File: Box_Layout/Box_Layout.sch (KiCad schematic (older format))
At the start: 32 parts, among them J1 Arduino_Mega_Header, X1 AMP967629, X2 DT04-12P

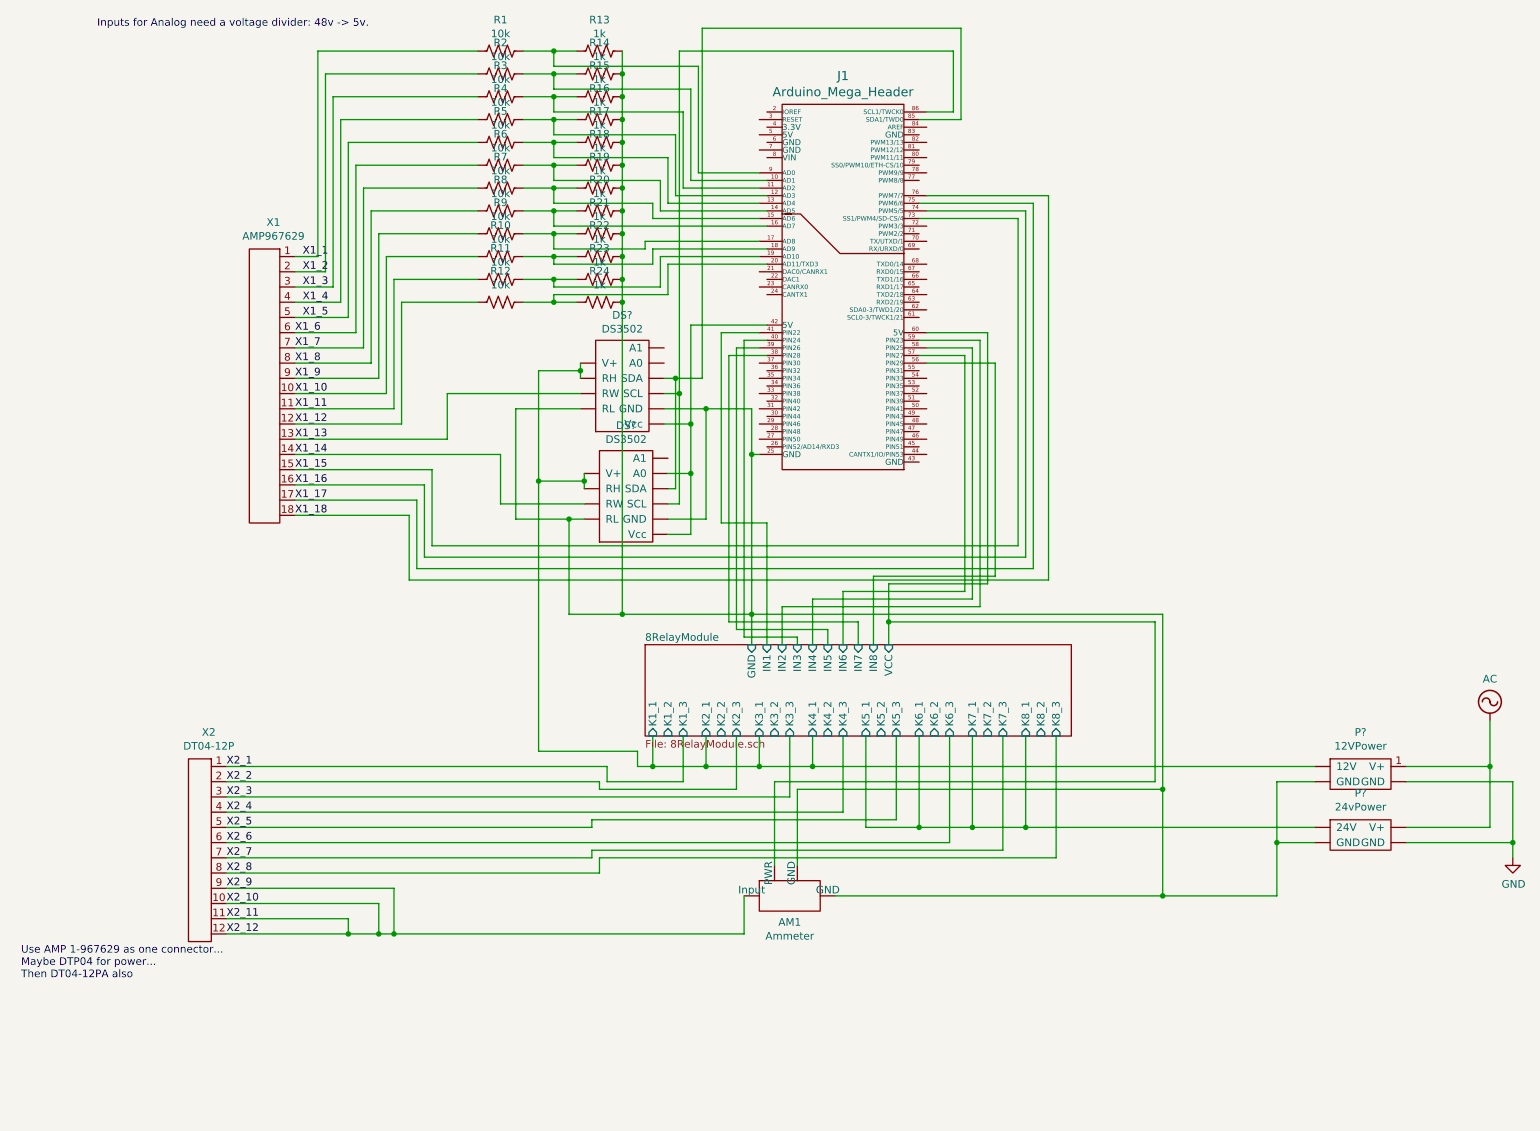
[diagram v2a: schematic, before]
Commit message: Changes to layout, and a bit to code.  Added a few tests.
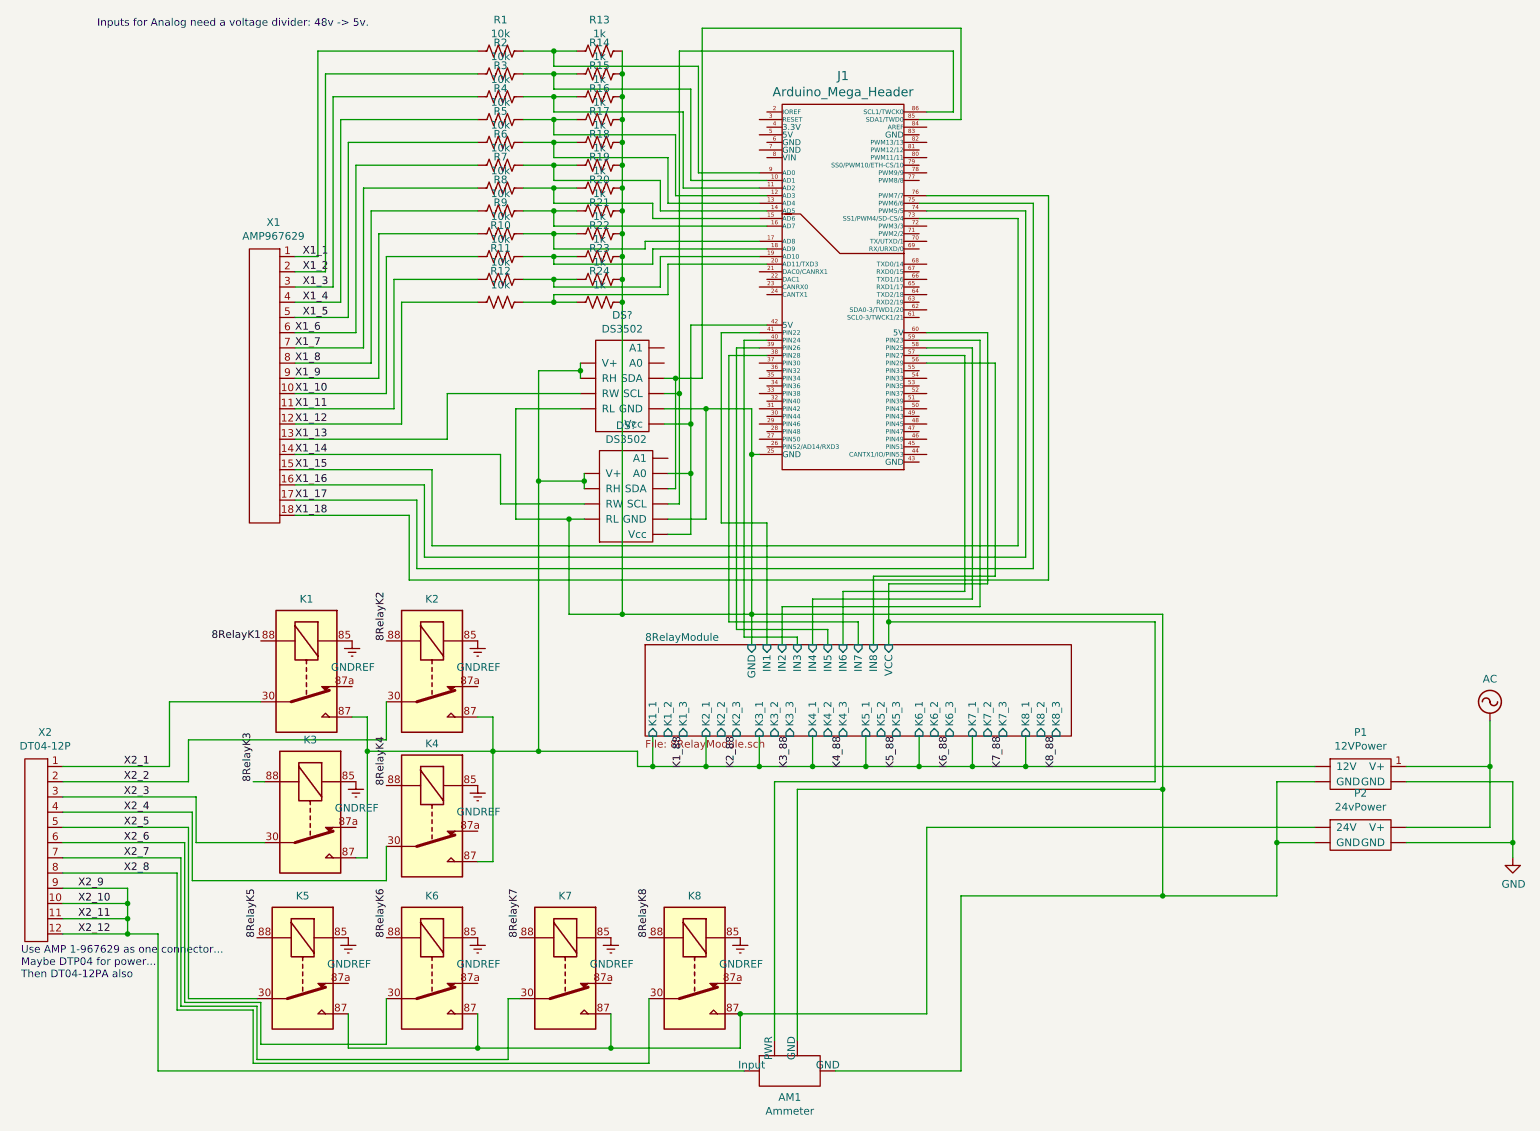
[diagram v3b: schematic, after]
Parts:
- added K1, K2, K3, K4, K5, K6, K7, K8: DIPxx-1Cxx-51x, Relay_THT:Relay_StandexMeder_DIP_LowProfile, symbol Relay:DIPxx-1Cxx-51x
- gave numbers to parts that had none: 2
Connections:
- net 8RelayModule/K5_1 is gone; now on net GND: P2.~ (V+)
- net 8RelayModule/K1_1: now also K1.87, K2.87, K3.87, K4.87
- net X2_1: now also K1.30, K1.8
- net X2_2: now also K2.30, K2.8
- net X2_3: now also K3.30, K3.8
- net X2_4: now also K4.30, K4.8
- net X2_5: now also K5.30, K5.8
- net X2_6: now also K6.30, K6.8
- net X2_7: now also K7.30, K7.8
- net X2_8: now also K8.30, K8.8
- new net: DS?.~ (Vcc), DS?.~ (Vcc), J1.42 (5V)
- new net: DS?.~ (Vcc), DS?.~ (Vcc), J1.85 (SDA1/TWD0)
- new net: DS?.~ (Vcc), DS?.~ (Vcc), J1.86 (SCL1/TWCK0)
- new net: K5.87, K6.87, K7.87, K8.87, P2.~ (V+)
- new net 8RelayK1: K1.88
- new net 8RelayK2: K2.88
- new net 8RelayK3: K3.88
- new net 8RelayK4: K4.88
- new net 8RelayK5: K5.88
- new net 8RelayK6: K6.88
- new net 8RelayK7: K7.88
- new net 8RelayK8: K8.88
- new net GNDREF: K1.85, K2.85, K3.85, K4.85, K5.85, K6.85, K7.85, K8.85
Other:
- moved on the sheet: AM1, X2
